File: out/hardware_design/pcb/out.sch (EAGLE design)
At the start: 77 parts, among them T1 MMBT3904, T2 MMBT3904, T3 MMBT3904, U1 TL072CD, U2 TL072CD, U3 TL072CD, U4 NE5532D, U5 NE5532D

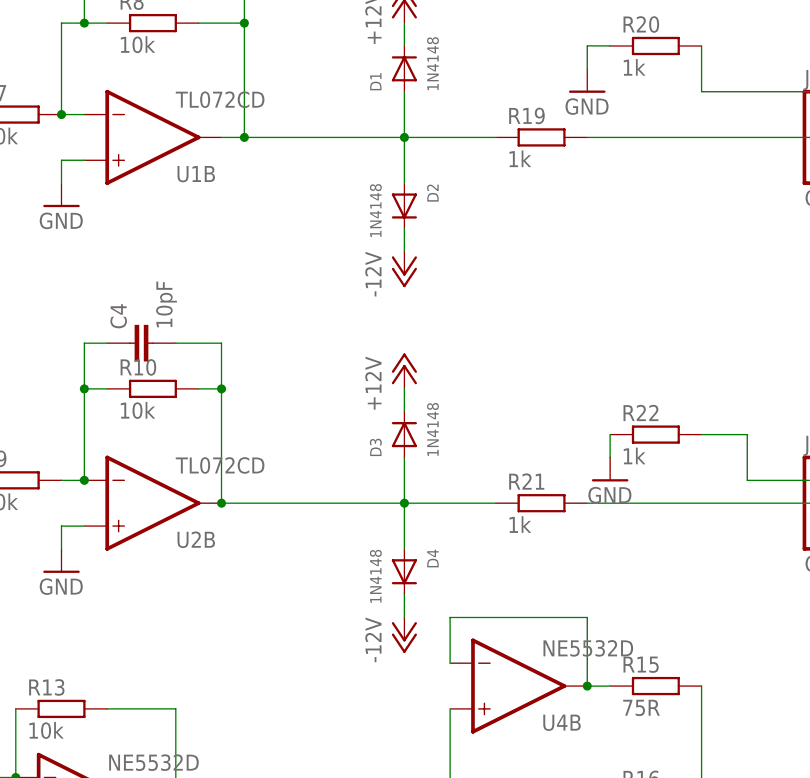
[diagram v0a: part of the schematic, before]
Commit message: Fix out oderso, implement menu scrolling i guess
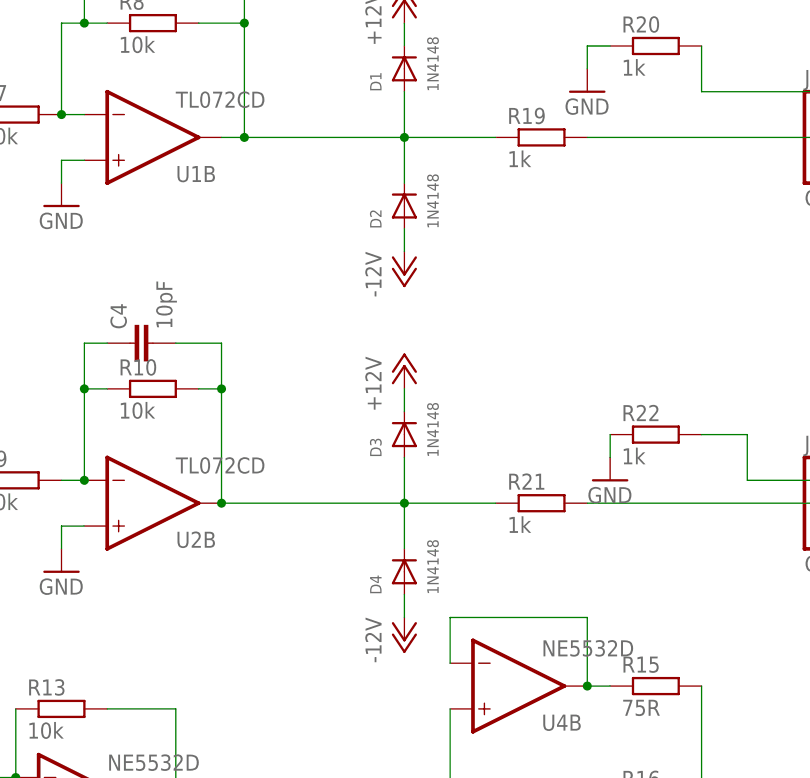
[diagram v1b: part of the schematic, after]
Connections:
- net -12V: now also D2.A, D4.A; no longer D2.C, D4.C
- net N$1: now also D2.C; no longer D2.A
- net N$2: now also D4.C; no longer D4.A
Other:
- moved on the sheet: D2, D4
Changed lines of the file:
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@@
 <attribute name="VALUE" x="146.05" y="71.12" size="1.27" layer="96" rot="R90"/>
 </instance>
-<instance part="D2" gate="G$1" x="142.24" y="58.42" smashed="yes" rot="R270">
-<attribute name="NAME" x="144.78" y="60.96" size="1.27" layer="95" rot="R270"/>
-<attribute name="VALUE" x="138.43" y="60.96" size="1.27" layer="96" rot="R270"/>
+<instance part="D2" gate="G$1" x="142.24" y="58.42" smashed="yes" rot="R90">
+<attribute name="NAME" x="139.7" y="55.88" size="1.27" layer="95" rot="R90"/>
+<attribute name="VALUE" x="146.05" y="55.88" size="1.27" layer="96" rot="R90"/>
 </instance>
 <instance part="D3" gate="G$1" x="142.24" y="33.02" smashed="yes" rot="R90">
@@
 <attribute name="VALUE" x="146.05" y="30.48" size="1.27" layer="96" rot="R90"/>
 </instance>
-<instance part="D4" gate="G$1" x="142.24" y="17.78" smashed="yes" rot="R270">
-<attribute name="NAME" x="144.78" y="20.32" size="1.27" layer="95" rot="R270"/>
-<attribute name="VALUE" x="138.43" y="20.32" size="1.27" layer="96" rot="R270"/>
+<instance part="D4" gate="G$1" x="142.24" y="17.78" smashed="yes" rot="R90">
+<attribute name="NAME" x="139.7" y="15.24" size="1.27" layer="95" rot="R90"/>
+<attribute name="VALUE" x="146.05" y="15.24" size="1.27" layer="96" rot="R90"/>
 </instance>
 <instance part="GND1" gate="1" x="10.16" y="66.04" smashed="yes">
@@
 <wire x1="142.24" y1="71.12" x2="142.24" y2="66.04" width="0.1524" layer="91"/>
 <junction x="142.24" y="66.04"/>
-<pinref part="D2" gate="G$1" pin="A"/>
-<wire x1="142.24" y1="60.96" x2="142.24" y2="66.04" width="0.1524" layer="91"/>
 <pinref part="C5" gate="G$1" pin="2"/>
 <wire x1="116.84" y1="83.82" x2="124.46" y2="83.82" width="0.1524" layer="91"/>
@@
 <wire x1="119.38" y1="78.74" x2="124.46" y2="78.74" width="0.1524" layer="91"/>
 <junction x="124.46" y="78.74"/>
+<pinref part="D2" gate="G$1" pin="C"/>
+<wire x1="142.24" y1="60.96" x2="142.24" y2="66.04" width="0.1524" layer="91"/>
 </segment>
 </net>
@@
 <wire x1="142.24" y1="30.48" x2="142.24" y2="25.4" width="0.1524" layer="91"/>
 <junction x="142.24" y="25.4"/>
-<pinref part="D4" gate="G$1" pin="A"/>
-<wire x1="142.24" y1="20.32" x2="142.24" y2="25.4" width="0.1524" layer="91"/>
 <pinref part="R10" gate="G$1" pin="2"/>
 <wire x1="119.38" y1="38.1" x2="121.92" y2="38.1" width="0.1524" layer="91"/>
@@
 <wire x1="121.92" y1="43.18" x2="121.92" y2="38.1" width="0.1524" layer="91"/>
 <junction x="121.92" y="38.1"/>
+<pinref part="D4" gate="G$1" pin="C"/>
+<wire x1="142.24" y1="20.32" x2="142.24" y2="25.4" width="0.1524" layer="91"/>
 </segment>
 </net>
@@
 </segment>
 <segment>
-<pinref part="P-2" gate="1" pin="-12V"/>
-<pinref part="D4" gate="G$1" pin="C"/>
-<wire x1="142.24" y1="12.7" x2="142.24" y2="15.24" width="0.1524" layer="91"/>
-</segment>
-<segment>
-<pinref part="P-3" gate="1" pin="-12V"/>
-<pinref part="D2" gate="G$1" pin="C"/>
-<wire x1="142.24" y1="53.34" x2="142.24" y2="55.88" width="0.1524" layer="91"/>
-</segment>
-<segment>
 <pinref part="D6" gate="G$1" pin="A"/>
 <wire x1="139.7" y1="-83.82" x2="142.24" y2="-83.82" width="0.1524" layer="91"/>
@@
 <junction x="144.78" y="-86.36"/>
 </segment>
-</net>
+<segment>
+<pinref part="P-2" gate="1" pin="-12V"/>
+<pinref part="D4" gate="G$1" pin="A"/>
+<wire x1="142.24" y1="12.7" x2="142.24" y2="15.24" width="0.1524" layer="91"/>
+</segment>
+<segment>
+<pinref part="P-3" gate="1" pin="-12V"/>
+<pinref part="D2" gate="G$1" pin="A"/>
+<wire x1="142.24" y1="53.34" x2="142.24" y2="55.88" width="0.1524" layer="91"/>
+</segment>
+</net>
